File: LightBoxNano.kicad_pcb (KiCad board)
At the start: 2 copper layers, 109.8 x 109.9 mm, 70 parts, among them J5V1 Conn_02 DNP, SW1 Knitter-Switch DRR4010

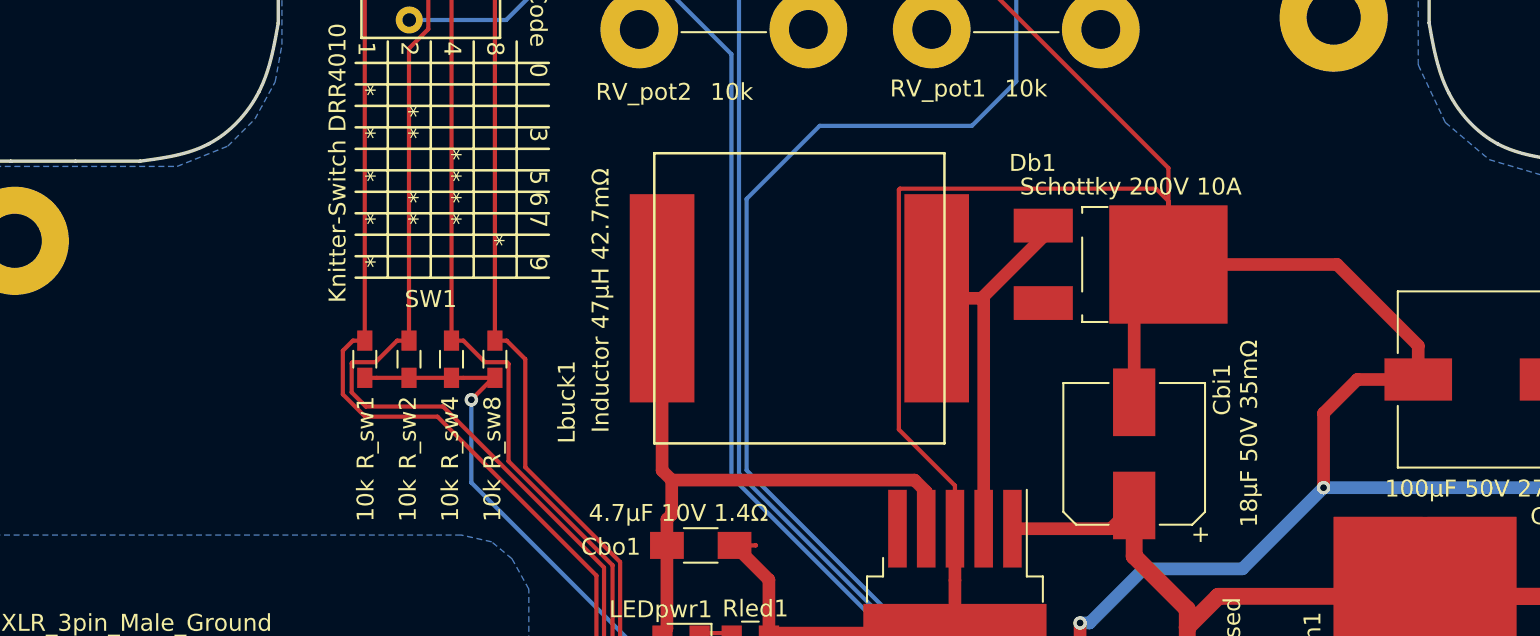
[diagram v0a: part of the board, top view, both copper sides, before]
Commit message: Add labels to PCB, plot output
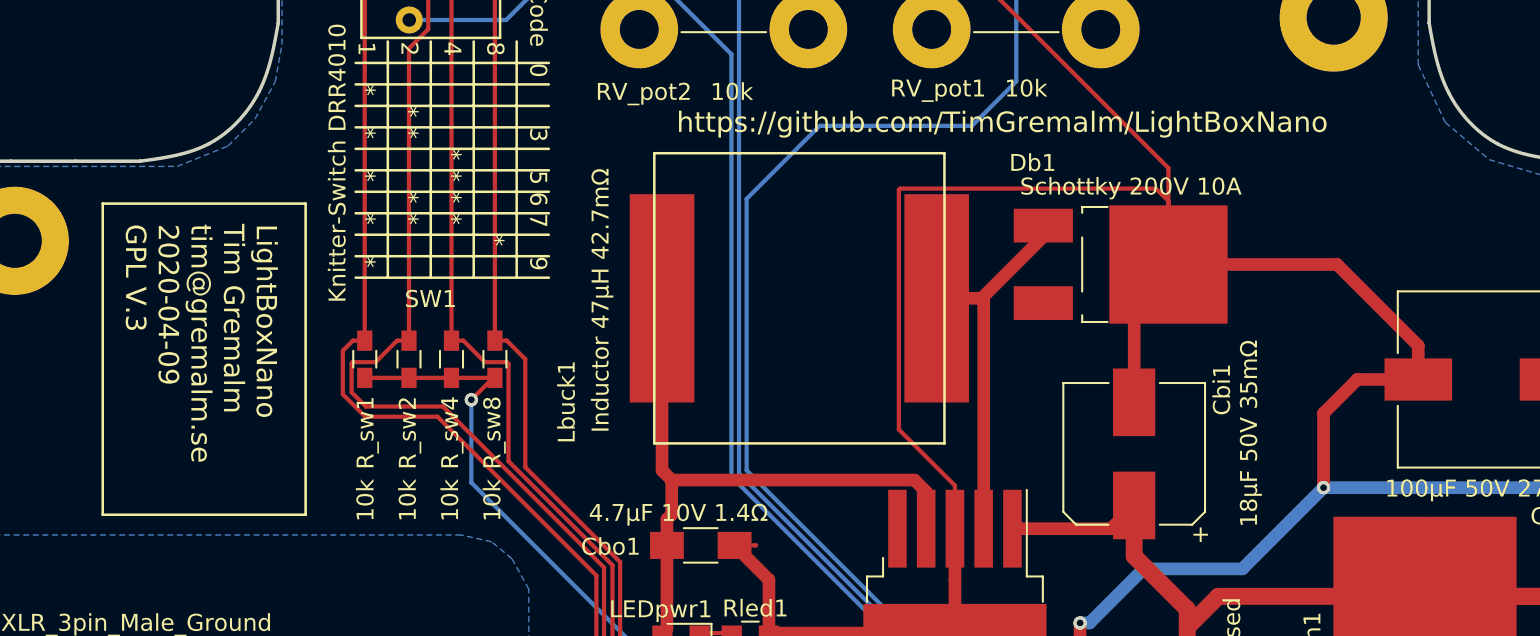
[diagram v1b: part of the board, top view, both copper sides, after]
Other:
- board text added: "LightBoxNano Tim Gremalm tim@gremalm.se 2020-04-09 GPL V.3"
- board text added: "https://github.com/TimGremalm/LightBoxNano"
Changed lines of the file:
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@@
   (general
     (thickness 1.6)
-    (drawings 169)
+    (drawings 175)
     (tracks 679)
     (zones 0)
@@
     (visible_elements 7FFFFFFF)
     (pcbplotparams
-      (layerselection 0x010fc_ffffffff)
+      (layerselection 0x010f0_ffffffff)
       (usegerberextensions false)
       (usegerberattributes false)
@@
       (outputformat 1)
       (mirror false)
-      (drillshape 1)
+      (drillshape 0)
       (scaleselection 1)
-      (outputdirectory ""))
+      (outputdirectory "output/"))
   )
   (net 0 "")
@@
       (effects (font (size 1 1) (thickness 0.15)))
     )
-    (fp_text value "Barrel Jack Switch 5A 2mm" (at -14.4 5.6) (layer F.Fab)
+    (fp_text value "Barrel Jack Switch 5A 2mm" (at 13.6 4.2) (layer F.Fab)
       (effects (font (size 1 1) (thickness 0.15)))
     )
@@
       (net 3 +5V) (solder_mask_margin 0.1))
   )
+  (gr_line (start 99.8 69.8) (end 99.8 51.4) (layer F.SilkS) (width 0.15))
+  (gr_line (start 111.8 69.8) (end 99.8 69.8) (layer F.SilkS) (width 0.15))
+  (gr_line (start 111.8 51.4) (end 111.8 69.8) (layer F.SilkS) (width 0.15))
+  (gr_line (start 99.8 51.4) (end 111.8 51.4) (layer F.SilkS) (width 0.15))
+  (gr_text "LightBoxNano\nTim Gremalm\ntim@gremalm.se\n2020-04-09\nGPL V.3" (at 105.6 52.6 270) (layer F.SilkS)
+    (effects (font (size 1.2 1.2) (thickness 0.15)) (justify left))
+  )
+  (gr_text https://github.com/TimGremalm/LightBoxNano (at 153 46.6) (layer F.SilkS)
+    (effects (font (size 1.2 1.2) (thickness 0.25)))
+  )
   (gr_curve (pts (xy 199.102977 50.22992) (xy 199.089517 50.148789) (xy 199.076056 50.067658) (xy 199.062599 49.986526)) (layer Edge.Cuts) (width 0.2))

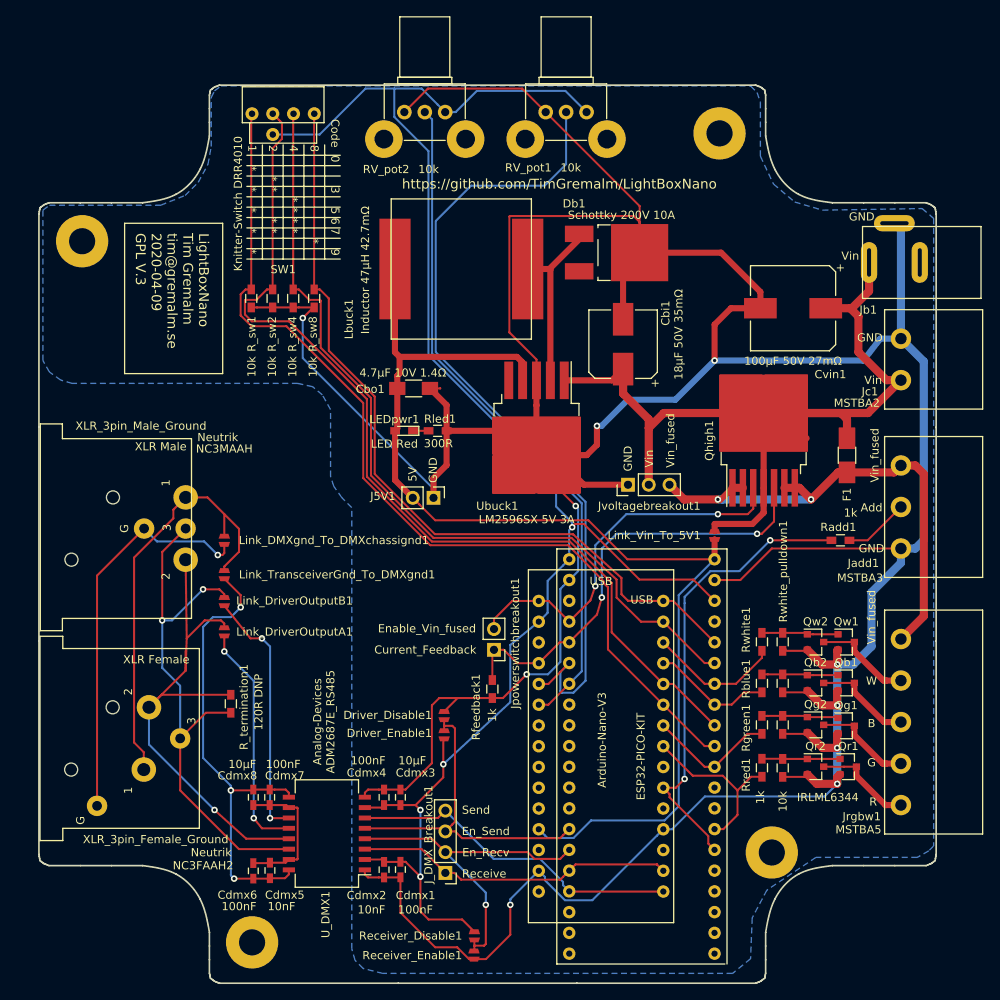
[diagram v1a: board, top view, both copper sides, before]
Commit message: Pretty labels on PCB
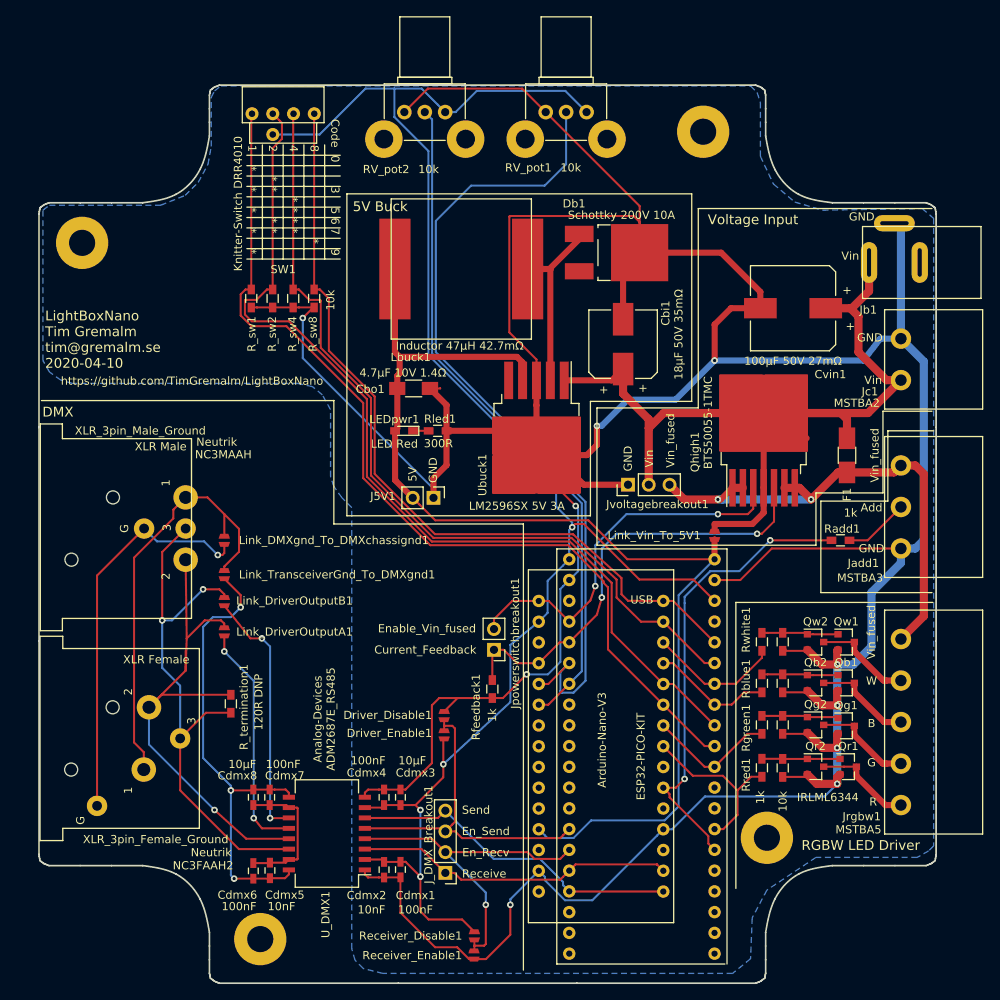
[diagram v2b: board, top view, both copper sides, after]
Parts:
- moved H3 2.01 mm to (170.6, 40.2)
- moved H4 1.90 mm to (178.4, 126.6)
- moved H2 1.08 mm to (116.4, 139.0)
- moved H1 0.20 mm to (94.6, 53.8)
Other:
- board text added: "+3.3V"
- board text added: "+3V3"
- board text added: "+5V"
- board text added: "1 DMX Gnd"
- board text added: "2 DMX -"
- board text added: "25"
- board text added: "26"
- board text added: "3 DMX +"
- board text added: "3V3"
- board text added: "5V"
- board text added: "5V Buck"
- board text added: "A0"
- board text added: "A1"
- board text added: "A2"
- board text added: "A3"
- board text added: "A4"
- board text added: "A5"
- board text added: "A6"
- board text added: "A7"
- board text added: "AREF"
- board text added: "Add"
- board text added: "B"
- board text added: "Current_Feedback"
- board text added: "D0/RX"
- board text added: "D1/TX"
- board text added: "D10"
- board text added: "D11"
- board text added: "D12"
- board text added: "D13"
- board text added: "D2"
- board text added: "D3"
- board text added: "D4"
- board text added: "D5"
- board text added: "D6"
- board text added: "D7"
- board text added: "D8"
- board text added: "D9"
- board text added: "DMX"
- board text added: "EN"
- board text added: "En_Recv"
- board text added: "En_Send"
- board text added: "Enable_Vin_fused"
- board text added: "G"
- board text added: "GND"
- board text added: "IO0"
- board text added: "IO10"
- board text added: "IO12"
- board text added: "IO13"
- board text added: "IO14"
- board text added: "IO15"
- board text added: "IO18"
- board text added: "IO19"
- board text added: "IO2"
- board text added: "IO21"
- board text added: "IO22"
- board text added: "IO23"
- board text added: "IO27"
- board text added: "IO32"
- board text added: "IO33"
- board text added: "IO34"
- board text added: "IO35"
- board text added: "IO37"
- board text added: "IO38"
- board text added: "IO4"
- board text added: "IO5"
- board text added: "IO9"
- board text added: "LightBoxNano Tim Gremalm tim@gremalm.se 2020-04-10"
- board text added: "LightBoxNano Tim Gremalm tim@gremalm.se https://github.com/TimGremalm/LightBoxNano"
- board text added: "POT_1"
- board text added: "POT_2"
- board text added: "R"
- board text added: "RESET"
- board text added: "RGBW LED Driver"
- board text added: "RXD0"
- board text added: "Receive"
- board text added: "Send"
- board text added: "Sens_VN"
- board text added: "Sens_VP"
- board text added: "SwCode1"
- board text added: "SwCode2"
- board text added: "SwCode4"
- board text added: "SwCode8"
- board text added: "TXD0"
- board text added: "VIN"
- board text added: "Vin"
- board text added: "Vin_fused"
- board text added: "Voltage Input"
- board text added: "W"
- board text removed: "LightBoxNano Tim Gremalm tim@gremalm.se 2020-04-09 GPL V.3"

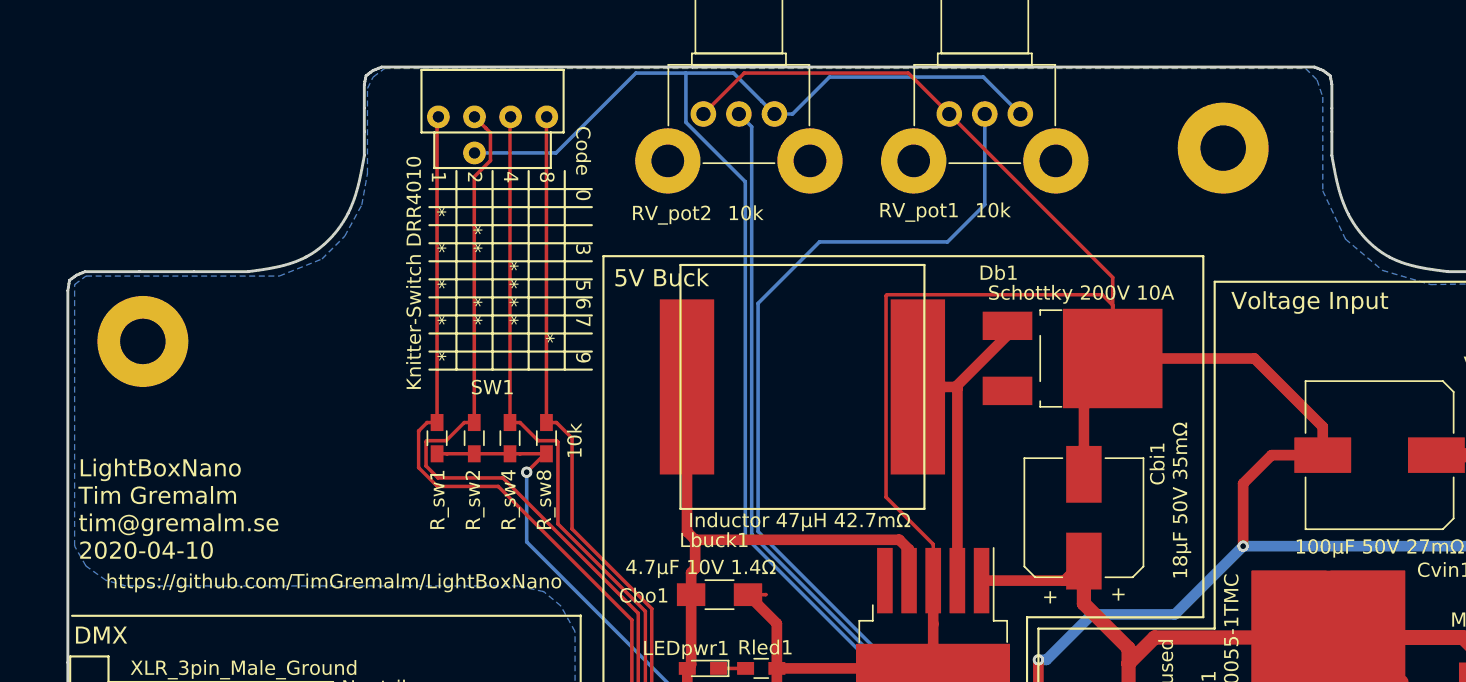
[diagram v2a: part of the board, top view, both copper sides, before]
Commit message: Smaller changes to labels on PCB
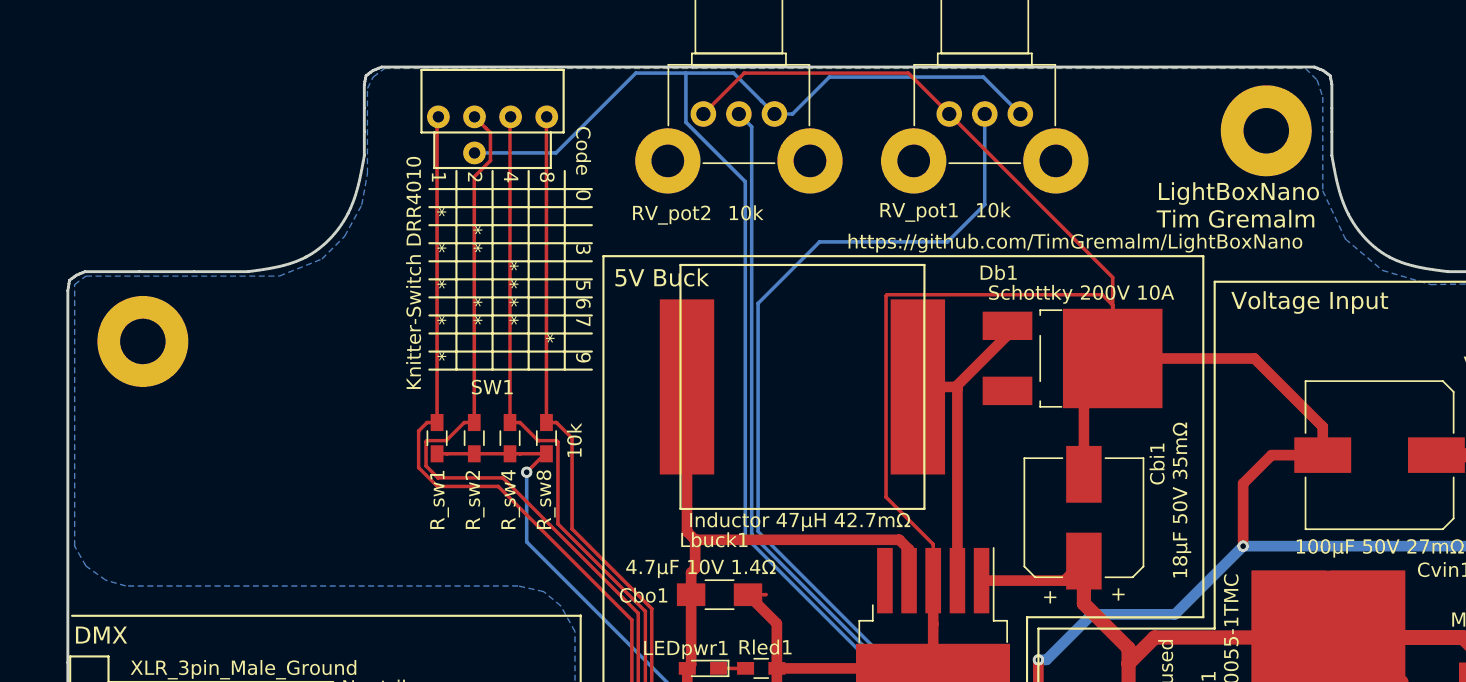
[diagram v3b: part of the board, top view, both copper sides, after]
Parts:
- moved H3 3.27 mm to (173.6, 39.0)
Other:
- board text added: "LightBoxNano Tim Gremalm"
- board text added: "LightBoxNano Tim Gremalm tim@gremalm.se 2020-04-10 https://github.com/TimGremalm/LightBoxNano"
- board text removed: "LightBoxNano Tim Gremalm tim@gremalm.se 2020-04-10"
- board text removed: "LightBoxNano Tim Gremalm tim@gremalm.se https://github.com/TimGremalm/LightBoxNano"
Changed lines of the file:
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@@
   )
   (module Mounting_Holes:MountingHole_3.2mm_M3_Pad (layer F.Cu)
-    (at 170.6 40.2)
+    (at 173.63 38.98)
     (descr "Mounting Hole 3.2mm, M3")
     (tags "mounting hole 3.2mm m3")
@@
     (effects (font (size 1 1) (thickness 0.15)) (justify mirror))
   )
-  (gr_text "LightBoxNano\nTim Gremalm\ntim@gremalm.se\nhttps://github.com/TimGremalm/LightBoxNano" (at 160.9 53.32) (layer B.SilkS)
+  (gr_text "LightBoxNano\nTim Gremalm\ntim@gremalm.se\n2020-04-10\nhttps://github.com/TimGremalm/LightBoxNano" (at 180.71 57.7) (layer B.SilkS)
     (effects (font (size 1.3 1.3) (thickness 0.15)) (justify left mirror))
   )
@@
     (effects (font (size 1.2 1.2) (thickness 0.25)))
   )
-  (gr_text https://github.com/TimGremalm/LightBoxNano (at 108.05 70.7) (layer F.SilkS)
+  (gr_text https://github.com/TimGremalm/LightBoxNano (at 160.18 46.8) (layer F.SilkS)
     (effects (font (size 1 1) (thickness 0.15)))
   )
@@
   (gr_line (start 127 87.2) (end 127 47.8) (layer F.SilkS) (width 0.15))
   (gr_line (start 127 87.2) (end 156.8 87.2) (layer F.SilkS) (width 0.15))
-  (gr_text "LightBoxNano\nTim Gremalm\ntim@gremalm.se\n2020-04-10" (at 90.07 65.63) (layer F.SilkS)
+  (gr_text "LightBoxNano\nTim Gremalm" (at 165.92 44.26) (layer F.SilkS)
     (effects (font (size 1.2 1.2) (thickness 0.15)) (justify left))
   )
